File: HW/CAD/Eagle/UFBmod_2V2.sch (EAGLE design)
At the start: 200 parts, among them J1411 ABRACON_ARJE-0034, T0551 MMBT2222, U0501 MIDAS_MCCOG21605B6W-FPTLWI, U0601 MAX5217, U0701 AT86RF215-ZU, U0711 ASVTX-13-D-26.000MHZ-I05-T, U0811 PE4259, U0821 RFX1010, U0881 B39871B3440U410, U0911 FT232HL, U1101 TPS53353, U1211 TPS62745DSSR, X0891 ANTENNATINY, X0895 ANTENNATINY, X1011 TTE_EN11-HSM, X1311 MOLEX 105017-0001, X1351 PHOENIX_1990067_1X8X2MM50_PTS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, X1361 PHOENIX_1990067_1X8X2MM50_PTS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

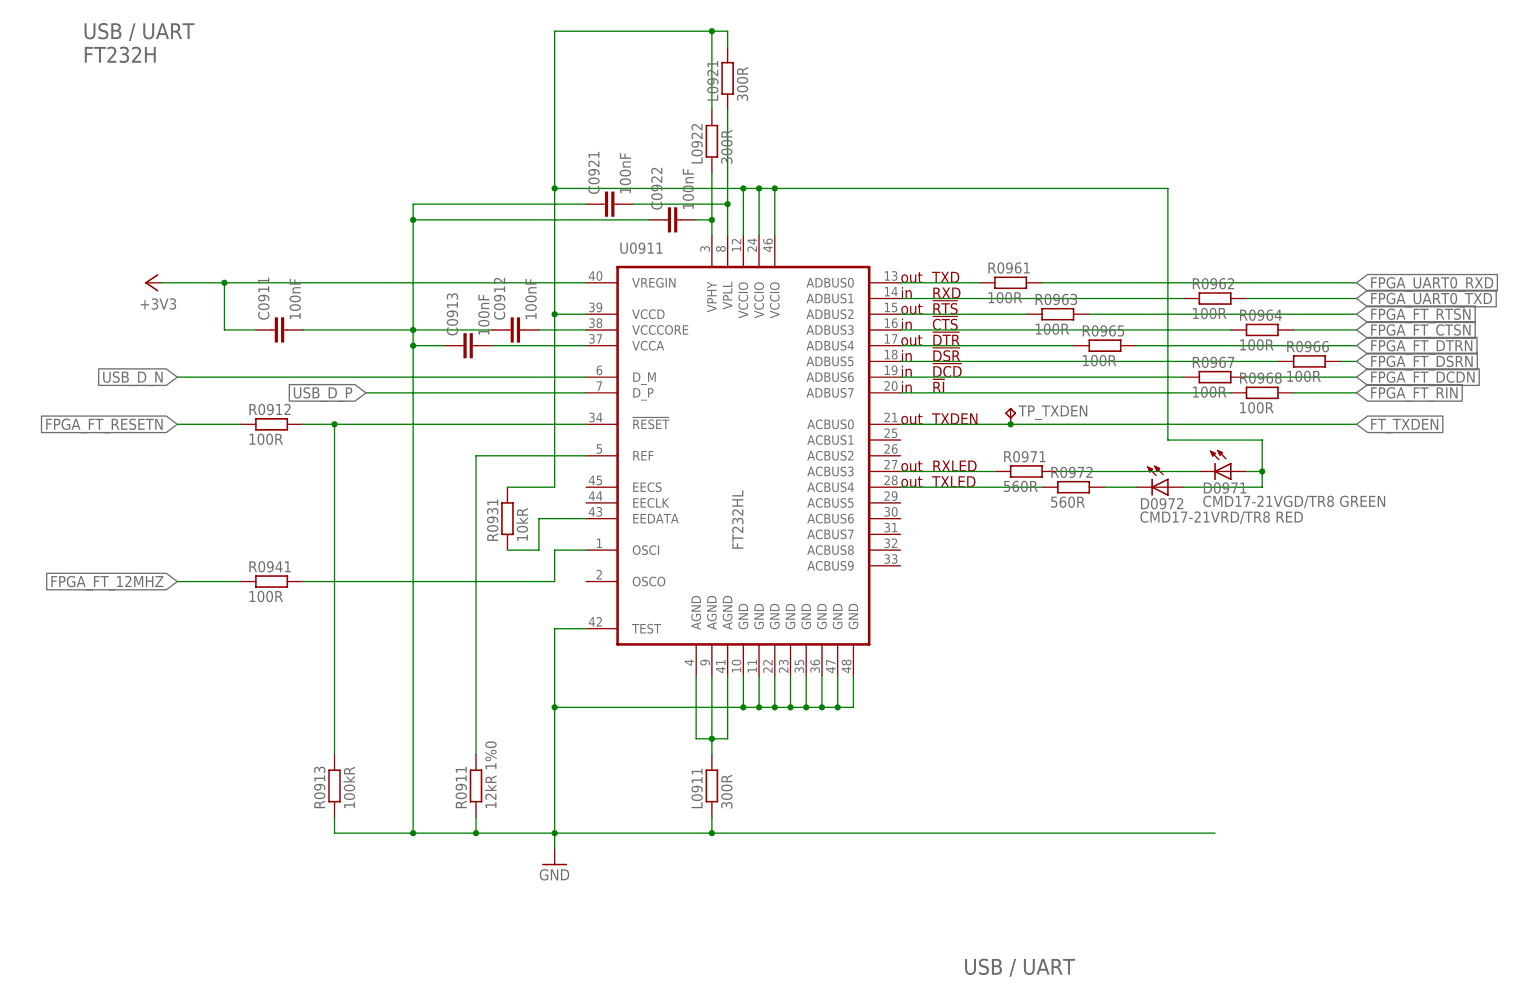
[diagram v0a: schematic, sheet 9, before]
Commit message: HW - Eagle - V2.2 - FT232H supply fixes, suppressor diodes to be added, layout still to do.
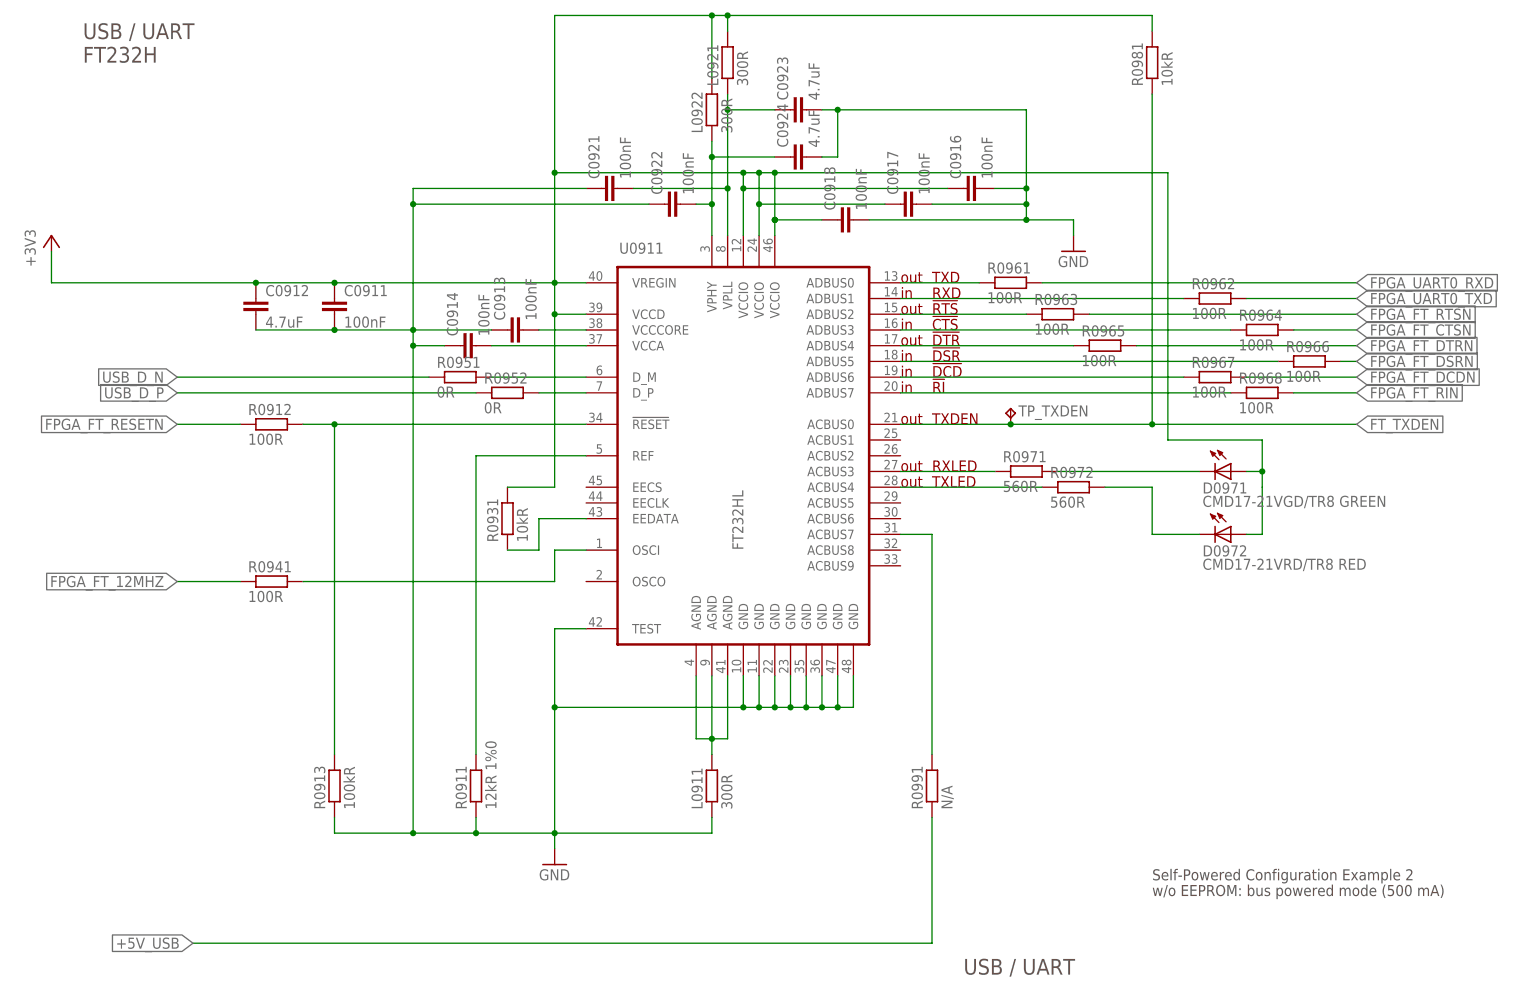
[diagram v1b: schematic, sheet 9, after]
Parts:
- added C0914, C0916, C0917, C0918: 100nF, df4iah_rcl:C-EUC0402
- added C0923, C0924: 4.7uF, df4iah_rcl:C-EUC0603
- added R0951, R0952: 0R, df4iah_rcl:R-EU_R0402
- added R0981: 10kR, df4iah_rcl:R-EU_R0402
- added R0991: N/A, df4iah_rcl:R-EU_R0402
- C0912: value 100nF -> 4.7uF; device df4iah_rcl:C-EUC0402 -> df4iah_rcl:C-EUC0603
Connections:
- net PMIC3V3_SW renamed PMIC2V5_SW
- removed net FT_VCCCORE: C0912.2, U0911.VCCCORE
- removed net FT_VCCD: D0971.A, D0972.A, L0921.2, L0922.2, R0931.2, U0911.VCCD, U0911.VCCIO@12, U0911.VCCIO@24, U0911.VCCIO@46
- new net FT_ACBUS7: R0991.2, U0911.ACBUS7
- new net FT_VCORE: C0913.2, U0911.VCCCORE
- new net N$1: R0951.2, U0911.D_M
- new net N$3: R0952.2, U0911.D_P
- net +3V3: now also C0912.1, C0916.1, C0917.1, C0918.1, D0971.A, D0972.A, L0921.2, L0922.2, R0931.2, R0981.2, U0911.VCCD, U0911.VCCIO@12, U0911.VCCIO@24, U0911.VCCIO@46
- net +5V_USB: now also R0991.1
- net FT_TXDEN: now also R0981.1
- net FT_VCCA: now also C0914.2; no longer C0913.2
- net FT_VPHY: now also C0924.1
- net FT_VPLL: now also C0923.1
- net GND: now also C0912.2, C0914.1, C0916.2, C0917.2, C0918.2, C0923.2, C0924.2; no longer C0912.1
- net USB_D_N: now also R0951.1; no longer U0911.D_M
- net USB_D_P: now also R0952.1; no longer U0911.D_P
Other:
- note added: "Self-Powered Configuration Example 2"
- note added: "TI SN75240PWR"
- note added: "w/o EEPROM: bus powered mode (500 mA)"
- moved on the sheet: C0911, C0912, C0913, C0921, C0922, D0972, L0921, L0922

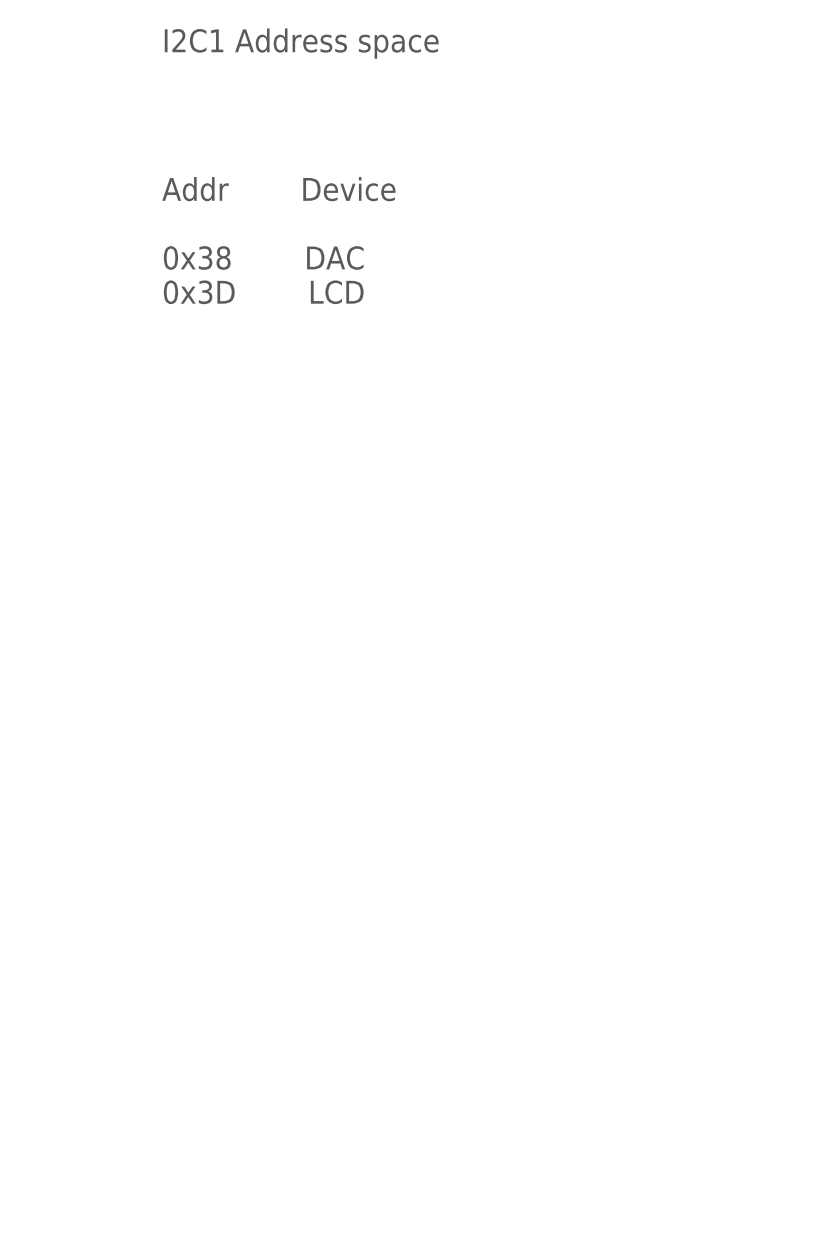
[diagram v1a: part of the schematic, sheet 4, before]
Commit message: HW - Eagle - V2.2 - reference voltage to be added, I2C address map fixed (V2.1 also)
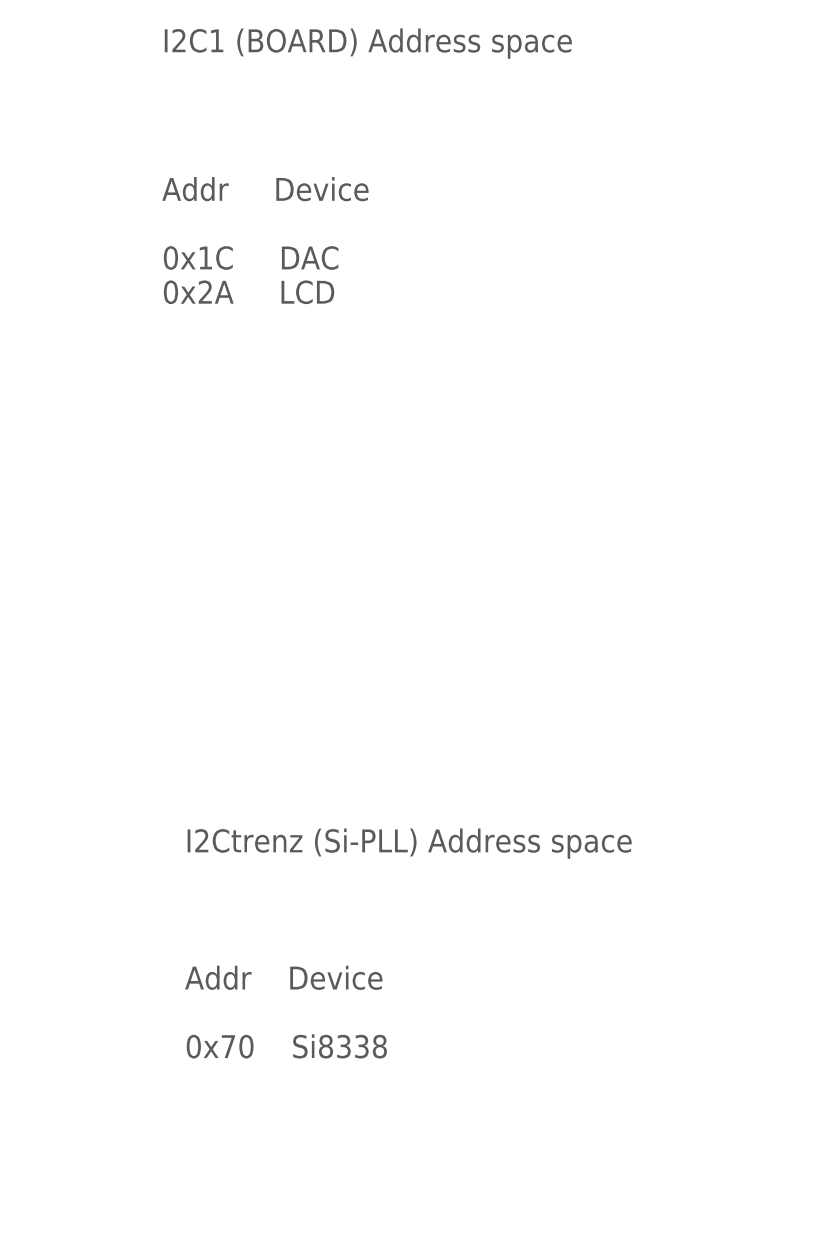
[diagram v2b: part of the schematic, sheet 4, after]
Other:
- note added: "Addr Device 0x1C DAC 0x2A LCD"
- note added: "Addr Device 0x70 Si8338"
- note added: "DAC for VCTCXO pull voltage I2C addr: 0x1C"
- note added: "I2C LCD module I2C addr: 0x2A"
- note added: "I2C1 (BOARD) Address space"
- note added: "I2Ctrenz (Si-PLL) Address space"
- note added: "Reminder: REF input needs voltage reference to minimize phase noise."
- note removed: "Addr Device 0x38 DAC 0x3D LCD"
- note removed: "DAC for VCTCXO pull voltage I2C addr: 0x38"
- note removed: "I2C LCD module I2C addr: 0x3D"
- note removed: "I2C1 Address space"
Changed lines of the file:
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@@
 <plain>
 <text x="165.1" y="15.24" size="2.54" layer="97" ratio="15">I2C: Termination</text>
-<text x="149.86" y="134.62" size="2.54" layer="97" ratio="15">Addr        Device
-0x38        DAC
-0x3D        LCD</text>
 <text x="22.86" y="162.56" size="2.54" layer="97" ratio="15">I2C Termination</text>
-<text x="149.86" y="162.56" size="2.54" layer="97" ratio="15">I2C1 Address space</text>
+<text x="149.86" y="134.62" size="2.54" layer="97" ratio="15">Addr     Device
+0x1C     DAC
+0x2A     LCD</text>
+<text x="149.86" y="162.56" size="2.54" layer="97" ratio="15">I2C1 (BOARD) Address space</text>
+<text x="152.4" y="73.66" size="2.54" layer="97" ratio="15">I2Ctrenz (Si-PLL) Address space</text>
+<text x="152.4" y="50.8" size="2.54" layer="97" ratio="15">Addr    Device
+0x70    Si8338</text>
 </plain>
 <instances>
@@
 <description>I2C LCD</description>
 <plain>
-<text x="22.86" y="162.56" size="2.54" layer="97" ratio="15">I2C LCD module
-I2C addr: 0x3D</text>
+<text x="22.86" y="160.02" size="2.54" layer="97" ratio="15">I2C LCD module
+I2C addr: 0x2A</text>
 <text x="165.1" y="15.24" size="2.54" layer="97" ratio="15">I2C: LCD</text>
 </plain>
@@
 <text x="109.22" y="104.14" size="1.778" layer="97">Iq=80uA</text>
 <text x="22.86" y="160.02" size="2.54" layer="97" ratio="15">DAC for VCTCXO pull voltage
-I2C addr: 0x38</text>
+I2C addr: 0x1C</text>
 <text x="165.1" y="15.24" size="2.54" layer="97" ratio="15">I2C: DAC</text>
+<text x="93.98" y="50.8" size="1.778" layer="97">Reminder: REF input needs voltage reference to minimize phase noise.</text>
 </plain>
 <instances>

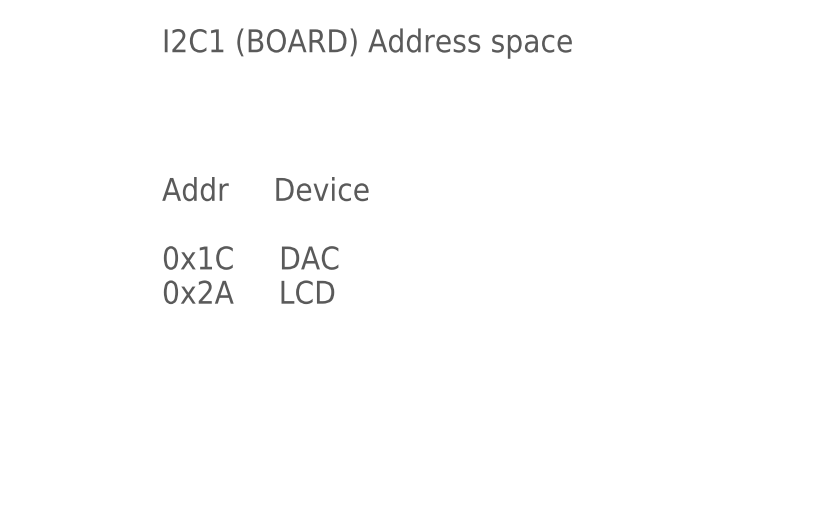
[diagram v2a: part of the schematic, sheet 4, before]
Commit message: HW - Eagle - V2.2 - I2C address map fixed again
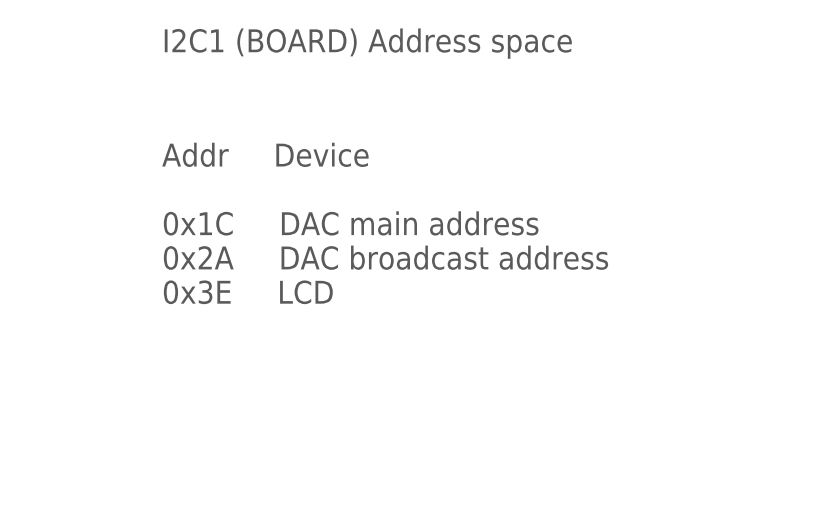
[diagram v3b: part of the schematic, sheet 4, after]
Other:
- note added: "Addr Device 0x1C DAC main address 0x2A DAC broadcast address 0x3E LCD"
- note added: "DAC for VCTCXO pull voltage I2C addr: 0x1C, I2C broadcast addr: 0x2A"
- note added: "I2C LCD module I2C addr: 0x3E"
- note removed: "Addr Device 0x1C DAC 0x2A LCD"
- note removed: "DAC for VCTCXO pull voltage I2C addr: 0x1C"
- note removed: "I2C LCD module I2C addr: 0x2A"
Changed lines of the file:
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@@
 <text x="22.86" y="162.56" size="2.54" layer="97" ratio="15">I2C Termination</text>
 <text x="149.86" y="134.62" size="2.54" layer="97" ratio="15">Addr     Device
-0x1C     DAC
-0x2A     LCD</text>
+0x1C     DAC main address
+0x2A     DAC broadcast address
+0x3E     LCD</text>
 <text x="149.86" y="162.56" size="2.54" layer="97" ratio="15">I2C1 (BOARD) Address space</text>
 <text x="152.4" y="73.66" size="2.54" layer="97" ratio="15">I2Ctrenz (Si-PLL) Address space</text>
@@
 <plain>
 <text x="22.86" y="160.02" size="2.54" layer="97" ratio="15">I2C LCD module
-I2C addr: 0x2A</text>
+I2C addr: 0x3E</text>
 <text x="165.1" y="15.24" size="2.54" layer="97" ratio="15">I2C: LCD</text>
 </plain>
@@
 <text x="109.22" y="104.14" size="1.778" layer="97">Iq=80uA</text>
 <text x="22.86" y="160.02" size="2.54" layer="97" ratio="15">DAC for VCTCXO pull voltage
-I2C addr: 0x1C</text>
+I2C addr: 0x1C, I2C broadcast addr: 0x2A</text>
 <text x="165.1" y="15.24" size="2.54" layer="97" ratio="15">I2C: DAC</text>
 <text x="93.98" y="50.8" size="1.778" layer="97">Reminder: REF input needs voltage reference to minimize phase noise.</text>
